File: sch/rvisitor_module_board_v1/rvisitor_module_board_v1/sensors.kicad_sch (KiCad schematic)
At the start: 18 parts, among them J10 CLIFF1, J11 CLIFF2, J12 CLIFF3, J5 DIST_SENS0, J5 DIST_SENS1, J5 DIST_SENS2, J5 DIST_SENS3, J9 CLIFF0, U7 CD74HC4067SM96, U8 CD74HC4067SM96

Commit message: [sch] rvisitor_module_board_v1 => power lines added
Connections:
- net VDDF renamed DIST_VIO
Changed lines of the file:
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@@
   (junction (at 191.77 43.18) (diameter 0) (color 0 0 0 0)
   )
+  (junction (at 213.36 71.12) (diameter 0) (color 0 0 0 0)
+  )
+  (junction (at 213.36 60.96) (diameter 0) (color 0 0 0 0)
+  )
+  (junction (at 213.36 76.2) (diameter 0) (color 0 0 0 0)
+  )
+  (junction (at 80.01 68.58) (diameter 0) (color 0 0 0 0)
+  )
+  (junction (at 80.01 60.96) (diameter 0) (color 0 0 0 0)
+  )
+  (junction (at 186.69 43.18) (diameter 0) (color 0 0 0 0)
+  )
   (junction (at 52.07 39.37) (diameter 0) (color 0 0 0 0)
   )
-  (junction (at 213.36 71.12) (diameter 0) (color 0 0 0 0)
-  )
-  (junction (at 213.36 60.96) (diameter 0) (color 0 0 0 0)
-  )
-  (junction (at 213.36 76.2) (diameter 0) (color 0 0 0 0)
-  )
-  (junction (at 80.01 68.58) (diameter 0) (color 0 0 0 0)
-  )
-  (junction (at 80.01 60.96) (diameter 0) (color 0 0 0 0)
-  )
-  (junction (at 186.69 43.18) (diameter 0) (color 0 0 0 0)
-  )
   (junction (at 213.36 63.5) (diameter 0) (color 0 0 0 0)
   )
@@
     (stroke (width 0) (type default))
   )
+  (wire (pts (xy 52.07 30.48) (xy 52.07 39.37))
+    (stroke (width 0) (type default))
+  )
   (wire (pts (xy 218.44 45.72) (xy 215.9 45.72))
     (stroke (width 0) (type default))
@@
   )
   (wire (pts (xy 80.01 73.66) (xy 80.01 76.2))
-    (stroke (width 0) (type default))
-  )
-  (wire (pts (xy 52.07 39.37) (xy 52.07 31.75))
     (stroke (width 0) (type default))
   )
@@
   (label "CLIFF_DATA" (at 200.66 86.36 0) (fields_autoplaced)
     (effects (font (size 1.27 1.27)) (justify left bottom))
+  )
+  (label "DIST_VIO" (at 52.07 30.48 270) (fields_autoplaced)
+    (effects (font (size 1.27 1.27)) (justify right bottom))
   )
   (label "ECHO" (at 67.31 59.69 180) (fields_autoplaced)
@@
         )
       )
-    )
-  )
-  (symbol (lib_id "power:VDDF") (at 52.07 31.75 0) (unit 1)
-    (in_bom yes) (on_board yes) (dnp no) (fields_autoplaced)
-    (property "Reference" "#PWR026" (at 52.07 35.56 0)
-      (effects (font (size 1.27 1.27)) hide)
-    )
-    (property "Value" "VDDF" (at 52.07 26.67 0)
-      (effects (font (size 1.27 1.27)))
-    )
-    (property "Footprint" "" (at 52.07 31.75 0)
-      (effects (font (size 1.27 1.27)) hide)
-    )
-    (property "Datasheet" "" (at 52.07 31.75 0)
-      (effects (font (size 1.27 1.27)) hide)
-    )
-    (pin "1")
-    (instances
-      (project "rvisitor_module_board_v1"
-        (path "/41f1d4db-cae0-4c46-bd8a-b53a93ecadfd/57f62111-ef76-4d09-afd0-9269d183c817"
-          (reference "#PWR026") (unit 1)
-        )
-      )

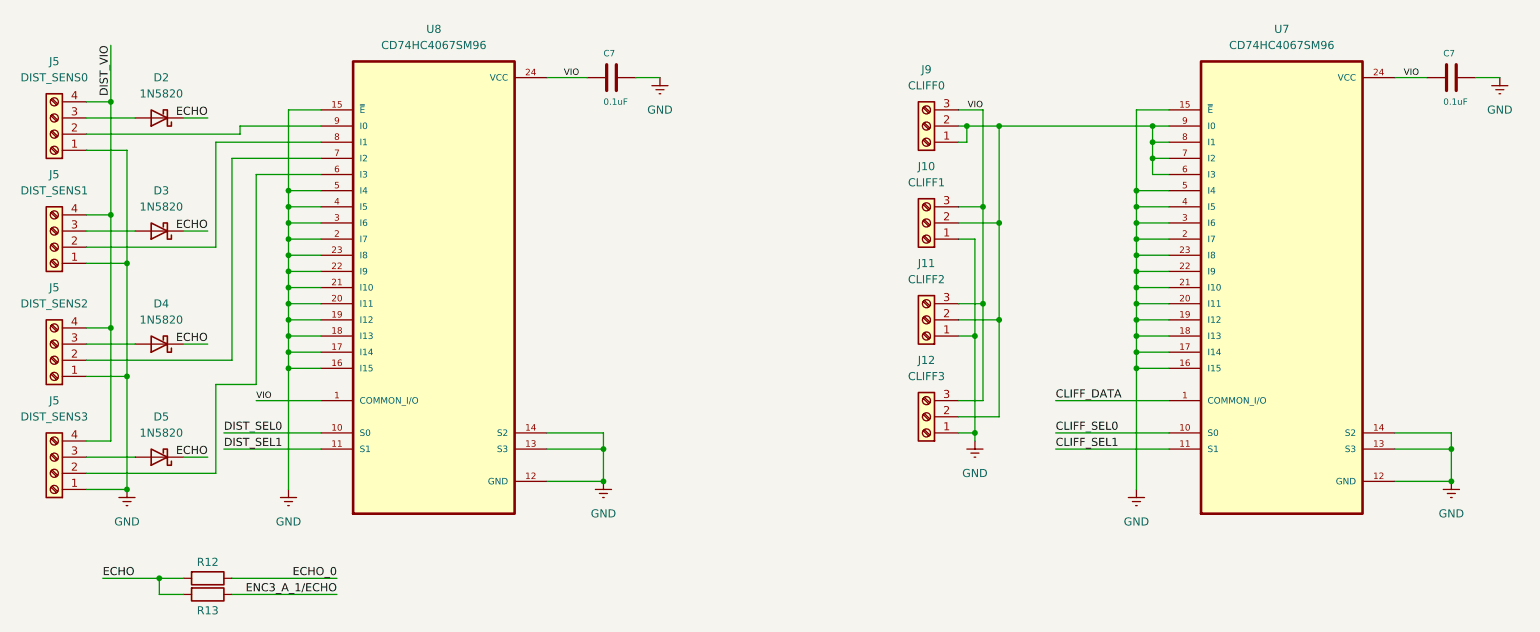
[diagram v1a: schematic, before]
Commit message: maket pcb start. maket add footprints. module_board_v1 start
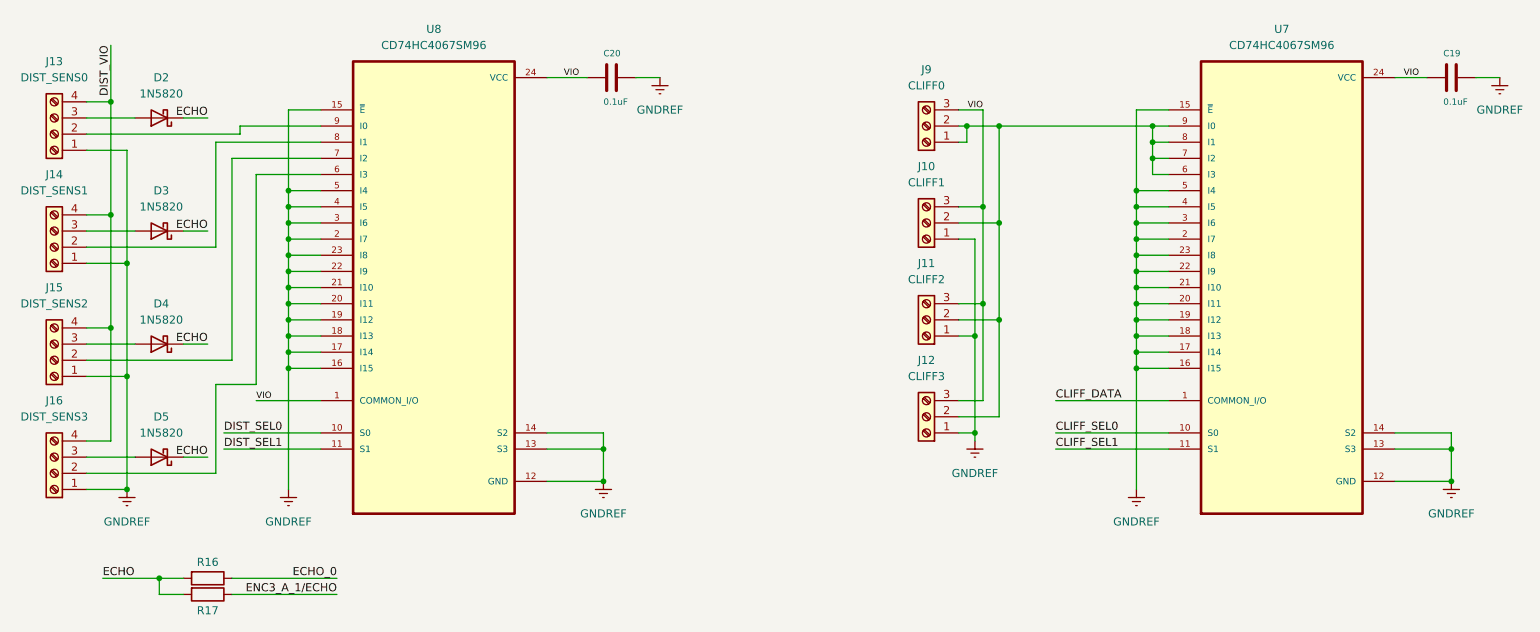
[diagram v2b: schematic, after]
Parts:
- renumbered C7 to C19, C7 to C20, J5 to J13, J5 to J14, J5 to J15, J5 to J16, R12 to R16, R13 to R17
